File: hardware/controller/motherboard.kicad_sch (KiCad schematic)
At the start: 54 parts, among them J10 TC2030, J2 Molex PicoBlade, J3 Conn_02x06_Odd_Even, J4 AFB10-S18LCA-00, J5 726386-2, J6 Conn_Coaxial_Small, J7 AFB10-S06LCA-00, J9 PinHeader 1x10 P1.00mm, Q1 AO3401A, SW90 SW_Push, U1 NRF52840, U2 nPM1300-QEAA, Y1 32MHz, Y2 32.768 kHz

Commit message: Update motherboard.kicad_sch
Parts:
- removed C34: 2.2u, symbol Device:C_Small
- added unit 4 of U1
- added unit 2 of U1
- added unit 5 of U1
- added unit 3 of U1
- U1: value NRF52840 -> nRF52840-QIAA; symbol nrf52840_qiaa_config5:root_0_nRF52840_QIAA_AltiumLib.DbLib -> ibm_m:nRF52840-QIAA
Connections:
- net D+: now also U1.AD6 (D+); no longer U1.AD6 (D+)
- net D-: now also U1.AD4 (D-); no longer U1.AD4 (D-)
- net GND: now also C1.2, C13.2, C17.2; no longer C1.1, C13.1, C17.1
- net SWCLK: now also U1.AA24 (SWDCLK); no longer U1.AA24 (SWDCLK)
- net SWDIO: now also U1.AC24 (SWDIO); no longer U1.AC24 (SWDIO)
- net at C18.2, Y2.1: now also U1.D2 (P0.00/XL1); no longer U1.F2 (P0.01/XL2)
- net at C2.2, Y1.1: now also U1.B24 (XC1); no longer U1.A23 (XC2)
- net at L2.2: now also U1.B3 (DCC); no longer U1.B3 (DCC)
- net at C5.2: now also U1.C1 (DEC1); no longer U1.C1 (DEC1)
- net at C11.2: now also U1.D23 (DEC3); no longer U1.D23 (DEC3)
- net at C3.1, L1.1: now also U1.H23 (ANT); no longer U1.H23 (ANT)
- net at C9.1: now also U1.N24 (DEC5); no longer U1.N24 (DEC5)
- net ANTENNA: no longer names the net of C22.1, C4.1, J6.1 (In), L1.2
- net DEC4: no longer names the net of C10.2, C15.1, C16.1, L3.1
- net DEC4: now also U1.B5 (DEC4), U1.E24 (DEC6); no longer U1.B5 (DEC4), U1.E24 (DEC6)
- new net: C13.1, U1.A18 (DEC2)
- new net: C17.1, U1.F2 (P0.01/XL2), Y2.2
- new net: C1.1, U1.A23 (XC2), Y1.3
- no-connect marks 11 -> 10
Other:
- note removed: "not req for Fxx and later"
- moved on the sheet: BT1, C1, C10, C11, C12, C13, C14, C15, C16, C17, C18, C2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

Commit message: feat(controller): nRF52840 pins for I2C, PMIC_INT, LED_EN, SWO, RESET
SDA P0.13, SCL P0.14, PMIC_INT P1.01, LED_EN P1.02, SWO P1.00,
P0.18/RESET to SW90. Changelog: P5, P6, F1, F2, M3 applied; M2 partial
(J10 pin 3 still on GND).
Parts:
- R10, R11, R12: symbol Device:R -> Device:R_Small
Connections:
- net LED_EN: now also U1.W24 (P1.02)
- net PMIC_INT: now also U1.Y23 (P1.01)
- net RESET: now also U1.AC13 (P0.18/RESET)
- net SCL: now also R11.2, U1.AC9 (P0.14); no longer R12.2
- net SDA: now also R12.2, U1.AD8 (P0.13); no longer R11.2
- net SWO: now also U1.AD22 (P1.00)
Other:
- moved on the sheet: R10, R11, R12

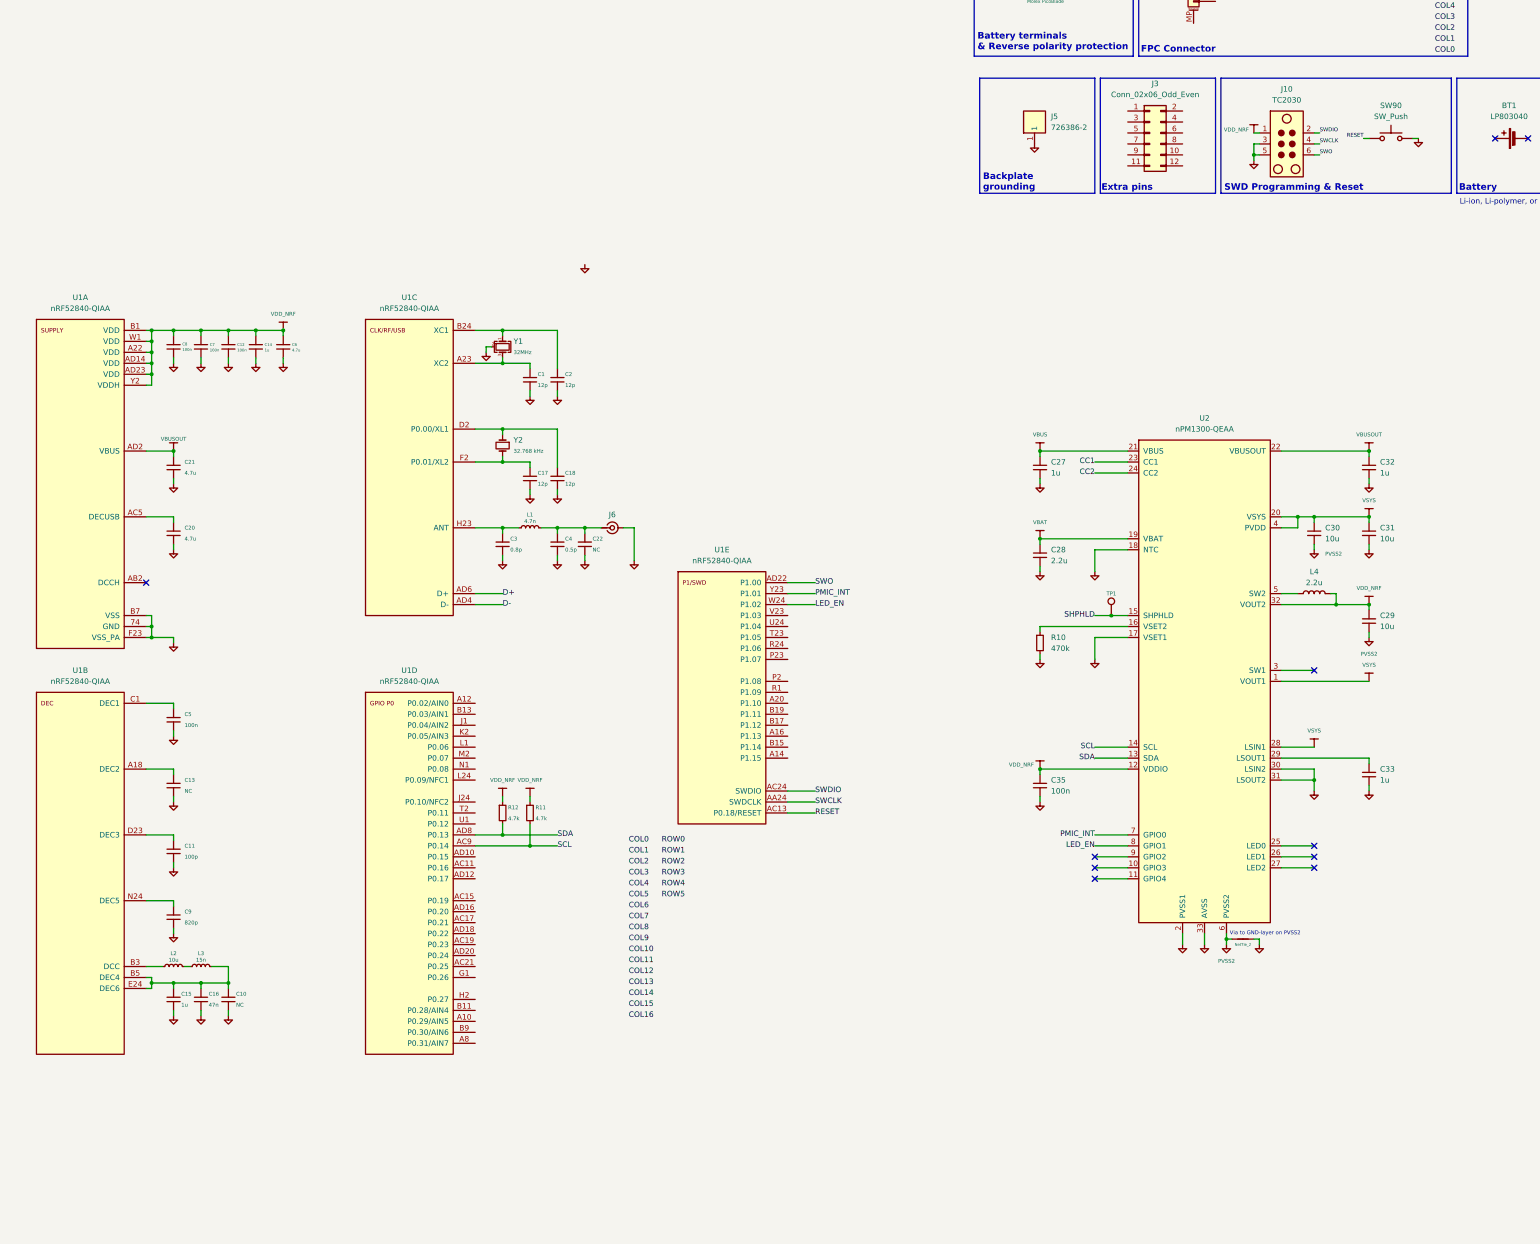
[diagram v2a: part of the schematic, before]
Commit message: feat(controller): Tag-Connect pin 3 on RESET (M2)
J10 pin 3 moved from GND to RESET with P0.18 and SW1 (renamed from
SW90). Changelog: M2 applied.
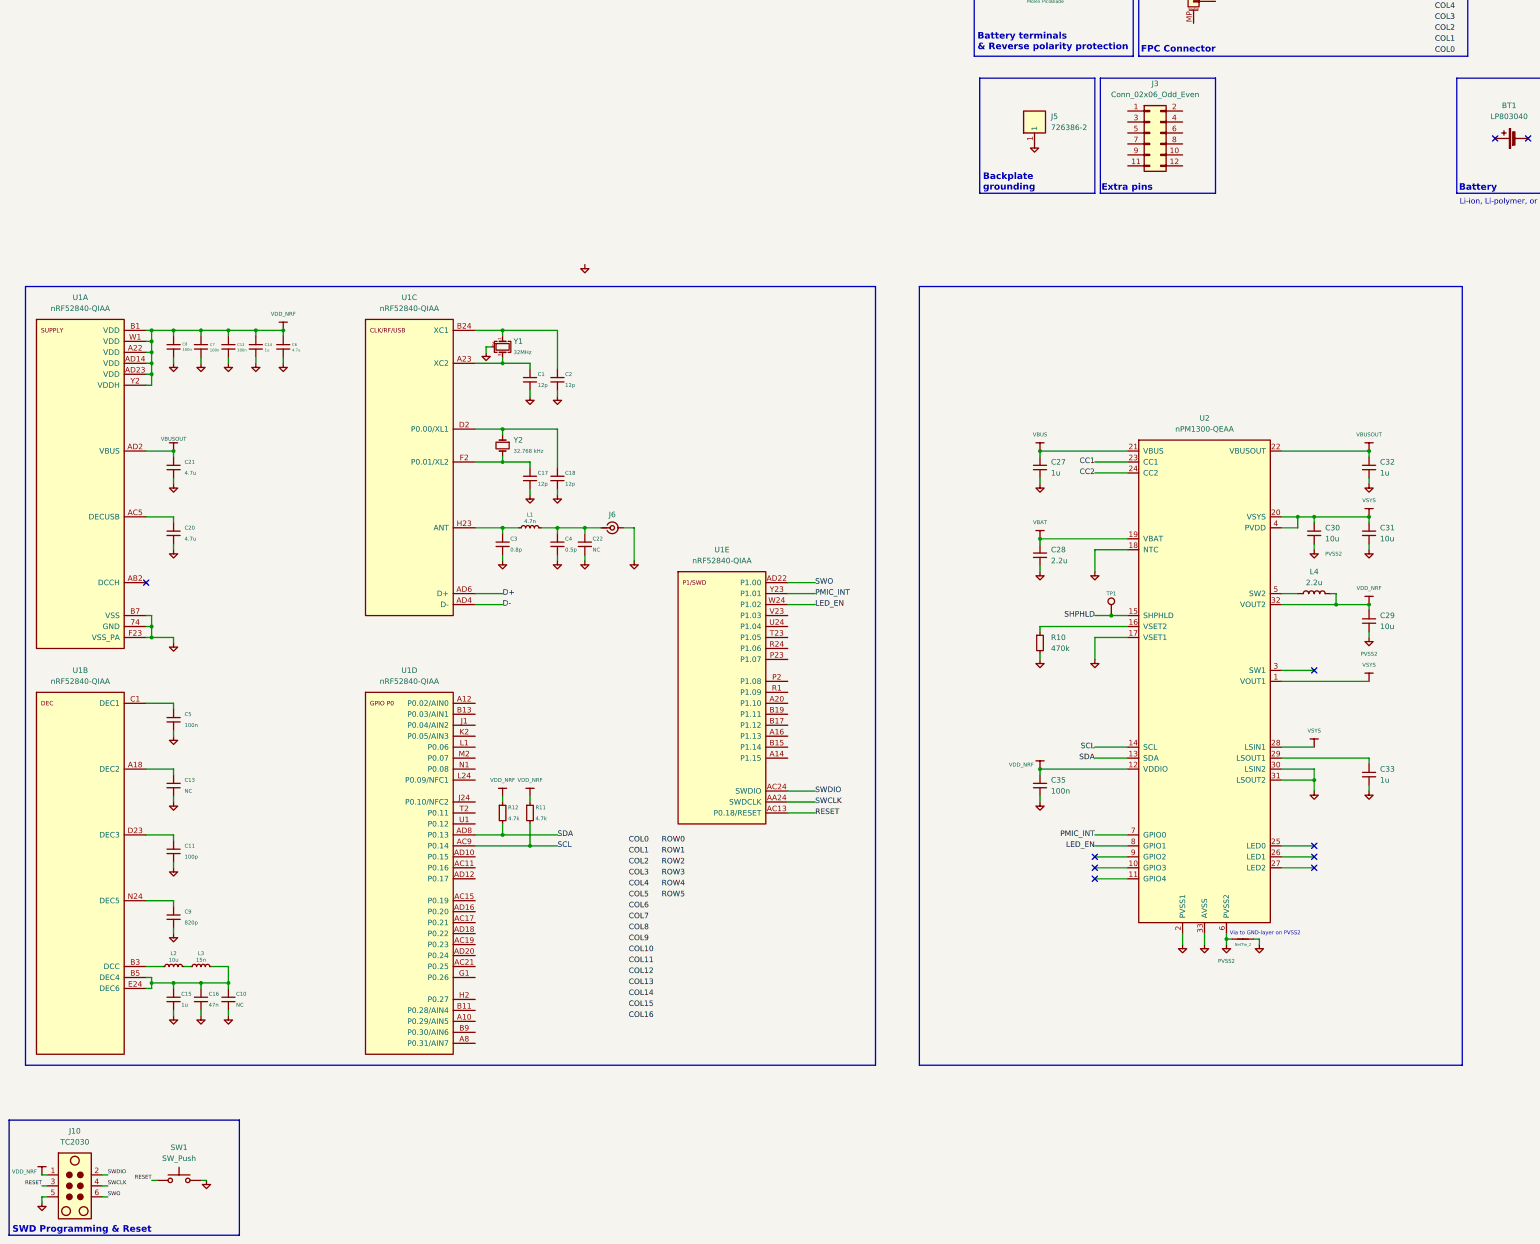
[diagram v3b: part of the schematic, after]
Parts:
- renumbered SW90 to SW1
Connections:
- net GND: no longer J10.3
- net RESET: now also J10.3
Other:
- moved on the sheet: J10, SW1
